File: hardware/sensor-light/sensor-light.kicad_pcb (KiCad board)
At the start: 2 copper layers, 95.2 x 33 mm, 15 parts, among them J2 PIR Sensor 2, J3 PIR Sensor 1, J4 PROG Header, J5 Light Sensor, J6 Power IN/OUT 12V, Q1 IRLML2502, SW1 Manual ON/OFF, U1 Reg 3.3V, U2 MSP430G2553IN20

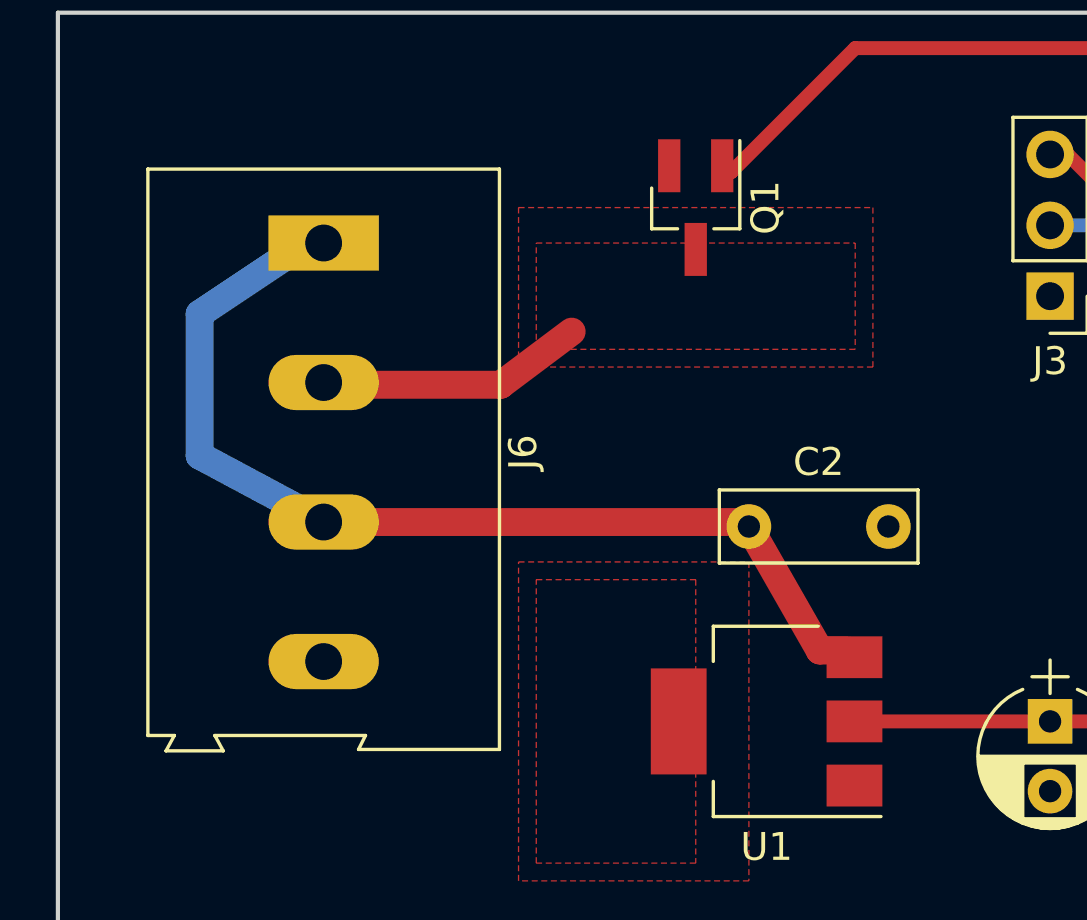
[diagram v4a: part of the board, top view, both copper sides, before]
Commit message: Change the power connector type
because I could not order AK300 :-\

Signed-off-by: Eugene Crosser <evgenii.cherkashin@profitbricks.com>
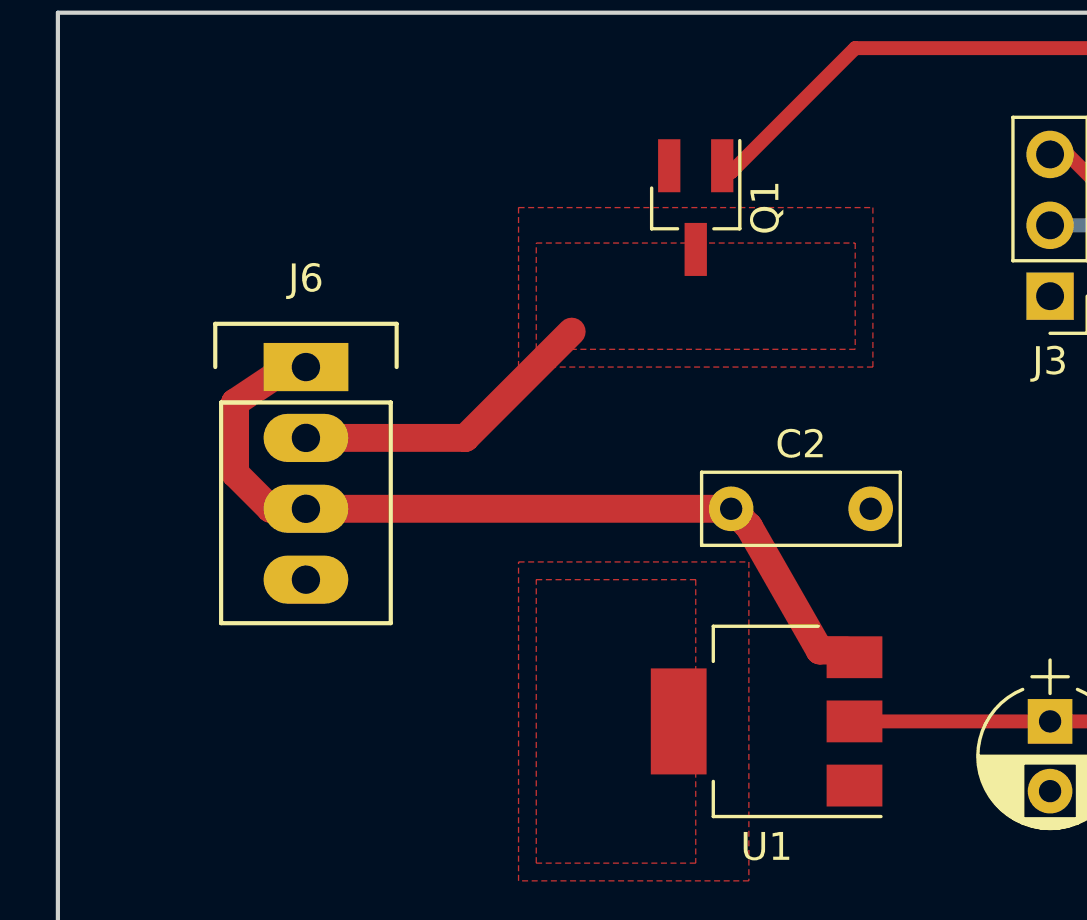
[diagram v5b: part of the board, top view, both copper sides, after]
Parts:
- D1: value Red -> Red 2mA
- D2: value Green -> Green 2mA
- J6: footprint Connectors:AK300-4 -> local:AKZ692_4
- R3: value 47 -> 681
- R4: value 27 -> 681
- moved J6 4.49 mm to (115.6, 113.7), turned to 0 degrees
- moved C2 0.90 mm to (130.8, 118.7)
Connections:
- U2 pad 10: (no net) -> Net-(U2-Pad10)
- U2 pad 11: (no net) -> Net-(U2-Pad11)
- U2 pad 15: (no net) -> Net-(U2-Pad15)
- U2 pad 18: (no net) -> Net-(U2-Pad18)
- U2 pad 19: (no net) -> Net-(U2-Pad19)
- U2 pad 3: (no net) -> Net-(U2-Pad3)
- U2 pad 7: (no net) -> Net-(U2-Pad7)
- U2 pad 8: (no net) -> Net-(U2-Pad8)
- U2 pad 9: (no net) -> Net-(U2-Pad9)
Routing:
- net Net-(C2-Pad1): track 37.4 -> 32.3 mm
- net Net-(J6-Pad2): track 9.96 -> 10.9 mm
